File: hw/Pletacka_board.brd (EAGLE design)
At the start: 75 x 60 mm, 59 parts, among them U1 LM75BDP-NEW, U2 EL357N(A)(TA)-G, U3 EL357N(A)(TA)-G, U4 EL357N(A)(TA)-G, U5 EL357N(A)(TA)-G, U6 TPS54231D

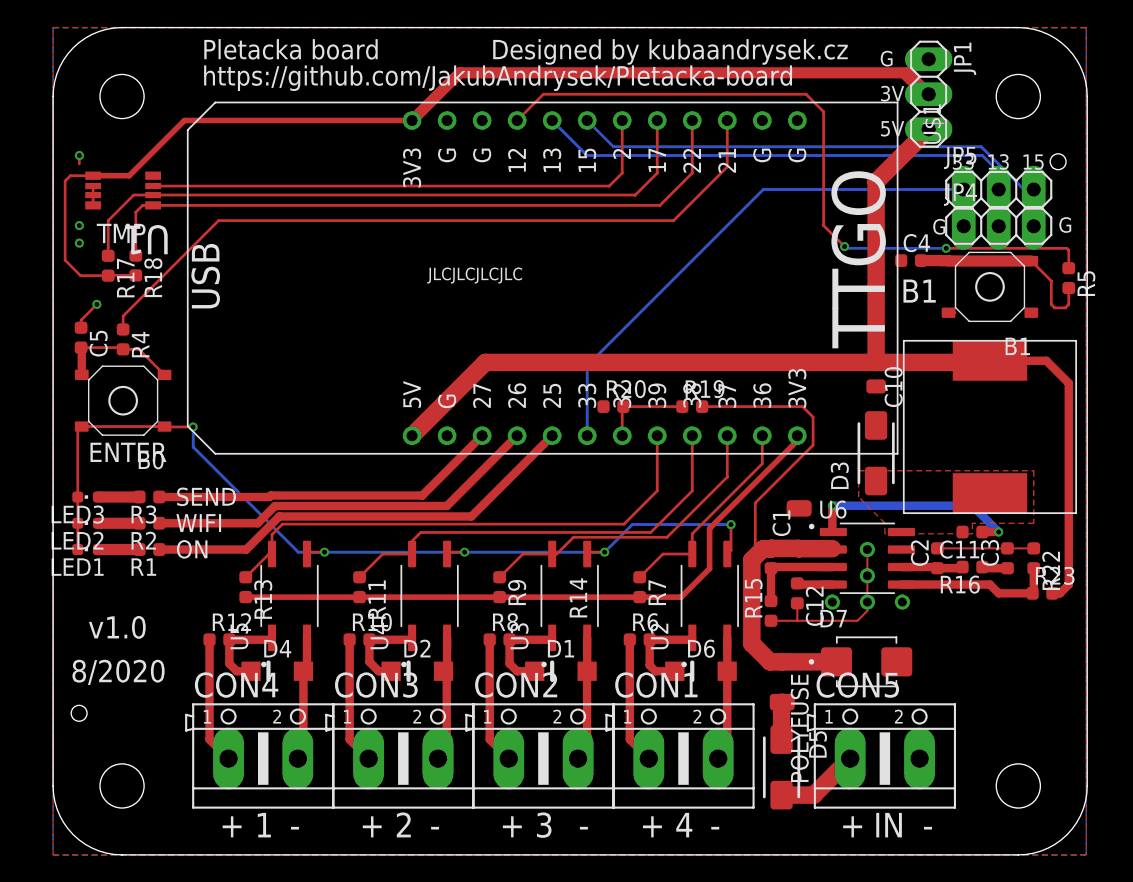
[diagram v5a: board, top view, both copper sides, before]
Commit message: Fix ports rotation
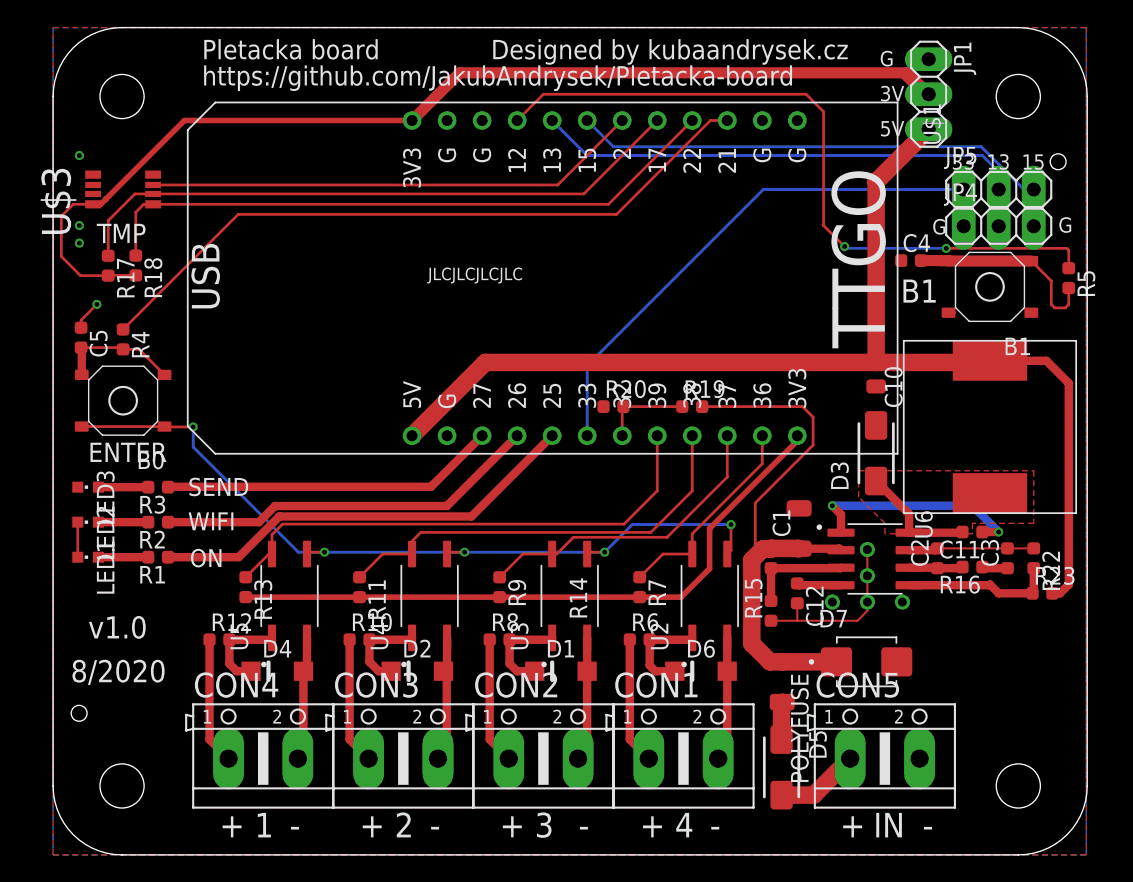
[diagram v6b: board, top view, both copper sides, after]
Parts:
- removed U1: LM75BDP-NEW, LM75BDP:SOT505-1
- added U$3: LM75BDP-NEW, LM75BDP:SOT505-1
- moved R3 0.96 mm to (7.62, 26.7)
- moved R1 0.84 mm to (7.62, 21.6)
- moved LED3 0.72 mm to (2.54, 26.7), turned to 180 degrees
- moved R2 0.64 mm to (7.62, 24.1)
- moved U6 0.56 mm to (59.6, 21.5), turned to 270 degrees
- moved LED1 0.55 mm to (2.54, 21.6), turned to 180 degrees
- moved LED2 0.08 mm to (2.54, 24.1), turned to 180 degrees
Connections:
- net +3V3: now also U$3.8; no longer U1.8
- net GND: now also U$3.4, U$3.5, U$3.6, U$3.7; no longer U1.4, U1.5, U1.6, U1.7
- net TMP_OS: now also U$3.3; no longer U1.3
- net TMP_SCL: now also U$3.2; no longer U1.2
- net TMP_SDA: now also U$3.1; no longer U1.1
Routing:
- net PH: track 0.00 -> 8.63 mm
- net GND: track 93.0 -> 86.6 mm
- net BUTTON1: track 52.6 -> 50.1 mm
- net TMP_OS: track 38.2 -> 36.0 mm
- net TMP_SCL: track 47.6 -> 45.4 mm
- net TMP_SDA: track 48.5 -> 46.3 mm
- net LED_SEND: track 25.3 -> 24.3 mm
- net +3V3: track 159.3 -> 158.5 mm
- net LED_WIFI: track 28.6 -> 27.9 mm
- net N$2: track 2.97 -> 3.61 mm
- net N$12: track 2.97 -> 3.61 mm
- net N$1: track 2.97 -> 3.61 mm
- net SS: track 2.65 -> 3.22 mm
- net +24V: track 42.3 -> 42.9 mm
- net VSENSE: track 11.6 -> 11.1 mm
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
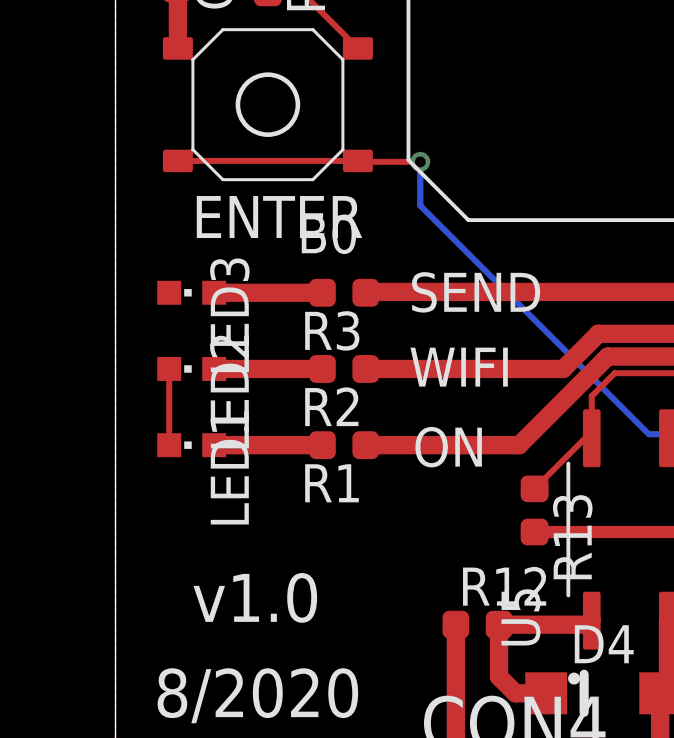
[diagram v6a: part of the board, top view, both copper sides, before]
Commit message: Fix ports rotation
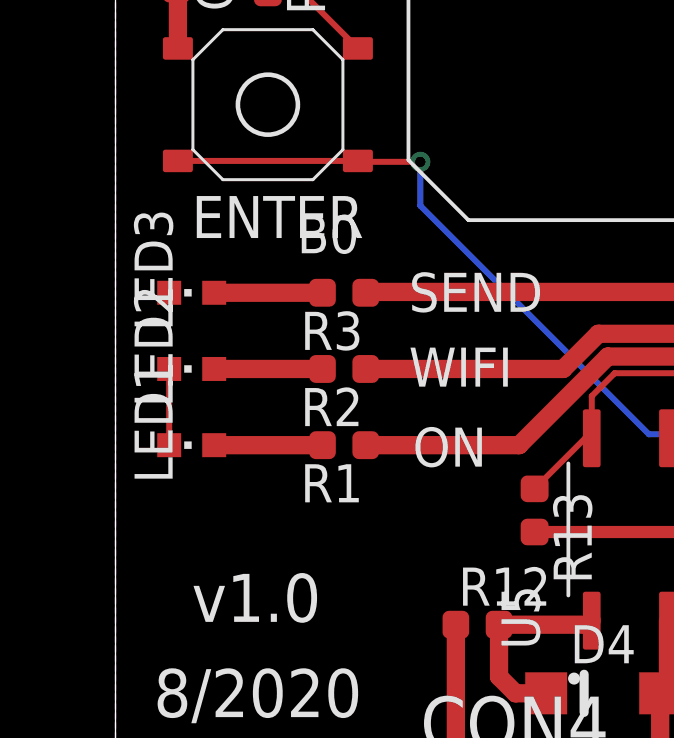
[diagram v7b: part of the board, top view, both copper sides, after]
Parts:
- turned LED1 to 0 degrees
- turned LED2 to 0 degrees
- turned LED3 to 0 degrees
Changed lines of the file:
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@@
 <attribute name="VALUE" x="0.127" y="38.147" size="1.27" layer="27" rot="R270"/>
 </element>
-<element name="LED1" library="led" package="CHIPLED_0603" package3d_urn="urn:adsk.eagle:package:15822/2" value="" x="2.54" y="21.59" smashed="yes" rot="R180">
-<attribute name="LCSC_ID" value="C2286" x="2.54" y="21.59" size="1.778" layer="27" rot="R180" display="off"/>
-<attribute name="NAME" x="3.175" y="22.86" size="1.27" layer="25" rot="R270"/>
-<attribute name="POPULARITY" value="28" x="2.54" y="21.59" size="1.778" layer="27" rot="R180" display="off"/>
-<attribute name="VALUE" x="0.635" y="22.86" size="1.27" layer="27" rot="R270"/>
-</element>
-<element name="LED2" library="led" package="CHIPLED_0603" package3d_urn="urn:adsk.eagle:package:15822/2" value="" x="2.54" y="24.13" smashed="yes" rot="R180">
-<attribute name="LCSC_ID" value="C2286" x="2.54" y="24.13" size="1.778" layer="27" rot="R180" display="off"/>
-<attribute name="NAME" x="3.175" y="25.4" size="1.27" layer="25" rot="R270"/>
-<attribute name="POPULARITY" value="28" x="2.54" y="24.13" size="1.778" layer="27" rot="R180" display="off"/>
-<attribute name="VALUE" x="0.635" y="25.4" size="1.27" layer="27" rot="R270"/>
-</element>
-<element name="LED3" library="led" package="CHIPLED_0603" package3d_urn="urn:adsk.eagle:package:15822/2" value="" x="2.54" y="26.67" smashed="yes" rot="R180">
-<attribute name="LCSC_ID" value="C2286" x="2.54" y="26.67" size="1.778" layer="27" rot="R180" display="off"/>
-<attribute name="NAME" x="3.175" y="27.94" size="1.27" layer="25" rot="R270"/>
-<attribute name="POPULARITY" value="28" x="2.54" y="26.67" size="1.778" layer="27" rot="R180" display="off"/>
-<attribute name="VALUE" x="0.635" y="27.94" size="1.27" layer="27" rot="R270"/>
+<element name="LED1" library="led" package="CHIPLED_0603" package3d_urn="urn:adsk.eagle:package:15822/2" value="" x="2.54" y="21.59" smashed="yes">
+<attribute name="LCSC_ID" value="C2286" x="2.54" y="21.59" size="1.778" layer="27" display="off"/>
+<attribute name="NAME" x="1.905" y="20.32" size="1.27" layer="25" rot="R90"/>
+<attribute name="POPULARITY" value="28" x="2.54" y="21.59" size="1.778" layer="27" display="off"/>
+<attribute name="VALUE" x="4.445" y="20.32" size="1.27" layer="27" rot="R90"/>
+</element>
+<element name="LED2" library="led" package="CHIPLED_0603" package3d_urn="urn:adsk.eagle:package:15822/2" value="" x="2.54" y="24.13" smashed="yes">
+<attribute name="LCSC_ID" value="C2286" x="2.54" y="24.13" size="1.778" layer="27" display="off"/>
+<attribute name="NAME" x="1.905" y="22.86" size="1.27" layer="25" rot="R90"/>
+<attribute name="POPULARITY" value="28" x="2.54" y="24.13" size="1.778" layer="27" display="off"/>
+<attribute name="VALUE" x="4.445" y="22.86" size="1.27" layer="27" rot="R90"/>
+</element>
+<element name="LED3" library="led" package="CHIPLED_0603" package3d_urn="urn:adsk.eagle:package:15822/2" value="" x="2.54" y="26.67" smashed="yes">
+<attribute name="LCSC_ID" value="C2286" x="2.54" y="26.67" size="1.778" layer="27" display="off"/>
+<attribute name="NAME" x="1.905" y="25.4" size="1.27" layer="25" rot="R90"/>
+<attribute name="POPULARITY" value="28" x="2.54" y="26.67" size="1.778" layer="27" display="off"/>
+<attribute name="VALUE" x="4.445" y="25.4" size="1.27" layer="27" rot="R90"/>
 </element>
 <element name="U$2" library="SWRB1204S-680MT" package="SWRB1204S" value="SWRB1204S" x="67.945" y="31.035" smashed="yes" rot="R90">
@@
 <contactref element="R1" pad="2"/>
 <contactref element="LED1" pad="A"/>
-<wire x1="6.9" y1="21.59" x2="3.29" y2="21.59" width="0.6096" layer="1"/>
+<wire x1="3.29" y1="21.59" x2="6.9" y2="21.59" width="0.6096" layer="1"/>
 </signal>
 <signal name="N$2">
 <contactref element="R2" pad="2"/>
 <contactref element="LED2" pad="A"/>
-<wire x1="6.9" y1="24.13" x2="3.29" y2="24.13" width="0.6096" layer="1"/>
+<wire x1="3.29" y1="24.13" x2="6.9" y2="24.13" width="0.6096" layer="1"/>
 </signal>
 <signal name="N$12">
 <contactref element="R3" pad="2"/>
 <contactref element="LED3" pad="A"/>
-<wire x1="6.9" y1="26.67" x2="3.29" y2="26.67" width="0.6096" layer="1"/>
+<wire x1="3.29" y1="26.67" x2="6.9" y2="26.67" width="0.6096" layer="1"/>
 </signal>
 <signal name="LED_WIFI">
